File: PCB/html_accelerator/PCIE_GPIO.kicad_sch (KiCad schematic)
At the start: 31 parts, among them U1 MCS9990, U3 CAT24C256YI-GT3, Y1 12MHz

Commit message: placement updates
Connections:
- net at R20.2, U1.29 (EE_SCL): now also U3.5 (SDA); no longer U3.6 (SCL)
- net at R20.2, U1.30 (EE_SDA): now also U3.6 (SCL); no longer U3.5 (SDA)
- net +3V3 renamed 3v3_filt
- net 3v3_filt: no longer R20.1
- new net +3V0: R20.1
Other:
- moved on the sheet: U3
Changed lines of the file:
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@@
     (stroke (width 0) (type default))
   )
+  (wire (pts (xy 41.91 25.4) (xy 40.64 25.4))
+    (stroke (width 0) (type default))
+  )
   (wire (pts (xy 40.64 41.91) (xy 40.64 53.34))
     (stroke (width 0) (type default))
@@
     (stroke (width 0) (type default))
   )
-  (wire (pts (xy 52.07 87.63) (xy 52.07 74.93))
+  (wire (pts (xy 52.07 73.66) (xy 52.07 87.63))
     (stroke (width 0) (type default))
   )
@@
     (stroke (width 0) (type default))
   )
-  (image (at 233.68 127) (scale 0.458951)
+  (image (at 233.68 127) (scale 0.972527)
     (data
       iVBORw0KGgoAAAANSUhEUgAAAt0AAAOOCAIAAABTODlIAAAAA3NCSVQICAjb4U/gAAAACXBIWXMA
-      ABYlAAAWJQFJUiTwAAAgAElEQVR4nOy9d9RlZXn3/7nusvcpz/NMowxtQECKUsSIXV9jNGLBgqiJ
+      ABXgAAAV4AGNVCw4AAAgAElEQVR4nOy9d9RlZXn3/7nusvcpz/NMowxtQECKUsSIXV9jNGLBgqiJ
       WBMTTTQWfDVGowaN4muiBhWx99hQCRYUIqiAKCJNijC0oTjDDNOecsred7neP/Y5zzwzQJK1fmv9
       fvhb57vOmvWcffa+275nX9/9va77ukW1D47sASQjGRREcQkiAJ7KksltAAHJYFiEsitkxy8BDLjU
@@
     )
   )
-  (image (at 238.76 73.66) (scale 0.546766)
+  (image (at 238.76 73.66) (scale 1.03777)
     (data
       iVBORw0KGgoAAAANSUhEUgAAAuwAAAE8CAIAAAAUlHMZAAAAA3NCSVQICAjb4U/gAAAACXBIWXMA
-      ABYlAAAWJQFJUiTwAAAgAElEQVR4nOy9ebwuR1ku+rxvVXV/31p7Z+9MEBISAZmUyxgwSgBFwQBX
+      ABXgAAAV4AGNVCw4AAAgAElEQVR4nOy9ebwuR1ku+rxvVXV/31p7Z+9MEBISAZmUyxgwSgBFwQBX
       HPDAUS8cjwiCGjgc1CCIHhSUweBlSnAERBEZhJigEoTILAQQEwhDIhCGE5LsZI9rfV93V9X7nj+q
       eviGtXeAyPV37ee3f3ut1V1dXVVdw1PP+1YVqUYAUAYABQgAlCAAIIBwuqaAcLoL4kg5LAOkAdB0
@@
     (effects (font (size 1.27 1.27)) (justify left bottom))
   )
-  (symbol (lib_id "power:+3V3") (at 40.64 25.4 0) (unit 1)
-    (in_bom yes) (on_board yes) (dnp no) (fields_autoplaced)
-    (property "Reference" "#PWR03" (at 40.64 29.21 0)
-      (effects (font (size 1.27 1.27)) hide)
-    )
-    (property "Value" "+3V3a_filt" (at 40.64 21.8981 0)
-      (effects (font (size 1.27 1.27)))
-    )
-    (property "Footprint" "" (at 40.64 25.4 0)
-      (effects (font (size 1.27 1.27)) hide)
-    )
-    (property "Datasheet" "" (at 40.64 25.4 0)
-      (effects (font (size 1.27 1.27)) hide)
-    )
-    (pin "1")
-    (instances
-      (project "html_accelerator"
-        (path "/12b3a7c9-141f-40ba-9ebb-094b58bfa6c7/3421334e-11b3-46c8-b0f2-353f0fa6f362"
-          (reference "#PWR03") (unit 1)
-        )
-        (path "/12b3a7c9-141f-40ba-9ebb-094b58bfa6c7/8c9bd1fc-c6d3-45cd-babe-9d9e8ea6549d"
-          (reference "#PWR051") (unit 1)
-        )
-        (path "/12b3a7c9-141f-40ba-9ebb-094b58bfa6c7/e5de870d-07a3-4698-84b8-c201bbab4843"
-          (reference "#PWR058") (unit 1)
-        )
-      )
+  (global_label "3v3_filt" (shape input) (at 41.91 25.4 0) (fields_autoplaced)
+    (effects (font (size 1.27 1.27)) (justify left))
+    (property "Intersheetrefs" "${INTERSHEET_REFS}" (at 51.8914 25.4 0)
+      (effects (font (size 1.27 1.27)) (justify left))
     )
   )
@@
     (pin "77")
     (pin "78")
+    (pin "81")
+    (pin "82")
     (pin "10")
     (pin "13")
@@
     (pin "54")
     (pin "57")
-    (pin "81")
-    (pin "82")
     (pin "100")
     (pin "102")
@@
     )
   )
-  (symbol (lib_name "MCS9990_1") (lib_id "html_accel_Symbols:MCS9990") (at 82.55 105.41 0) (unit 2)
+  (symbol (lib_id "html_accel_Symbols:MCS9990") (at 82.55 105.41 0) (unit 2)
     (in_bom yes) (on_board yes) (dnp no) (fields_autoplaced)
     (property "Reference" "U1" (at 98.425 101.1106 0)
@@
       (effects (font (size 1.27 1.27)) hide)
     )
-    (property "Datasheet" "5% Tolerance" (at 67.31 130.81 0)
+    (property "Datasheet" "~" (at 67.31 130.81 0)
       (effects (font (size 1.27 1.27)) hide)
     )
@@
     )
   )
-  (symbol (lib_id "power:+3V3") (at 100.33 45.72 0) (unit 1)
-    (in_bom yes) (on_board yes) (dnp no)
-    (property "Reference" "#PWR07" (at 100.33 49.53 0)
-      (effects (font (size 1.27 1.27)) hide)
-    )
-    (property "Value" "+3V3_aux" (at 100.33 42.2181 0)
-      (effects (font (size 1.27 1.27)))
-    )
-    (property "Footprint" "" (at 100.33 45.72 0)
-      (effects (font (size 1.27 1.27)) hide)
-    )
-    (property "Datasheet" "" (at 100.33 45.72 0)
-      (effects (font (size 1.27 1.27)) hide)
-    )
-    (pin "1")
-    (instances
-      (project "html_accelerator"
-        (path "/12b3a7c9-141f-40ba-9ebb-094b58bfa6c7/3421334e-11b3-46c8-b0f2-353f0fa6f362"
-          (reference "#PWR07") (unit 1)
-        )
-        (path "/12b3a7c9-141f-40ba-9ebb-094b58bfa6c7/e5de870d-07a3-4698-84b8-c201bbab4843"
-          (reference "#PWR059") (unit 1)
-        )
-      )
-    )
-  )
   (symbol (lib_id "Device:R_US") (at 69.85 49.53 0) (unit 1)
     (in_bom yes) (on_board yes) (dnp no)
@@
       (effects (font (size 1.27 1.27)) hide)
     )
-    (property "Datasheet" "12M20P2/49SMT" (at 59.69 123.19 0)
+    (property "Datasheet" "~" (at 59.69 123.19 0)
       (effects (font (size 1.27 1.27)) hide)
     )
@@
     )
   )
+  (symbol (lib_id "power:+3V0") (at 100.33 45.72 0) (unit 1)
+    (in_bom yes) (on_board yes) (dnp no) (fields_autoplaced)
+    (property "Reference" "#PWR011" (at 100.33 49.53 0)
+      (effects (font (size 1.27 1.27)) hide)
+    )
+    (property "Value" "+3V3_aux" (at 100.33 42.2181 0)
+      (effects (font (size 1.27 1.27)))
+    )
+    (property "Footprint" "" (at 100.33 45.72 0)
+      (effects (font (size 1.27 1.27)) hide)
+    )
+    (property "Datasheet" "" (at 100.33 45.72 0)
+      (effects (font (size 1.27 1.27)) hide)
+    )
+    (pin "1")
+    (instances
+      (project "html_accelerator"
+        (path "/12b3a7c9-141f-40ba-9ebb-094b58bfa6c7/3421334e-11b3-46c8-b0f2-353f0fa6f362"
+          (reference "#PWR011") (unit 1)
+        )
+        (path "/12b3a7c9-141f-40ba-9ebb-094b58bfa6c7/e5de870d-07a3-4698-84b8-c201bbab4843"
+          (reference "#PWR013") (unit 1)
+        )
+      )
+    )
+  )
   (symbol (lib_id "Device:R_US") (at 115.57 86.36 0) (unit 1)
     (in_bom yes) (on_board yes) (dnp no)
@@
       (effects (font (size 1.27 1.27)))
     )
-    (property "Footprint" "Package_SO:TSSOP-8_4.4x3mm_P0.65mm" (at 52.07 55.88 0)
+    (property "Footprint" "Package_SO:TSSOP-8_4.4x3mm_P0.65mm" (at 49.53 50.8 0)
       (effects (font (size 1.27 1.27)) hide)
     )
-    (property "Datasheet" "https://www.onsemi.cn/PowerSolutions/document/CAT24C256-D.PDF" (at 50.8 63.5 0)
+    (property "Datasheet" "https://www.onsemi.cn/PowerSolutions/document/CAT24C256-D.PDF" (at 52.07 50.8 0)
       (effects (font (size 1.27 1.27)) hide)
     )
@@
       (effects (font (size 1.27 1.27)) hide)
     )
-    (property "Datasheet" "5% tolerance" (at 52.07 130.81 0)
+    (property "Datasheet" "~" (at 52.07 130.81 0)
       (effects (font (size 1.27 1.27)) hide)
     )

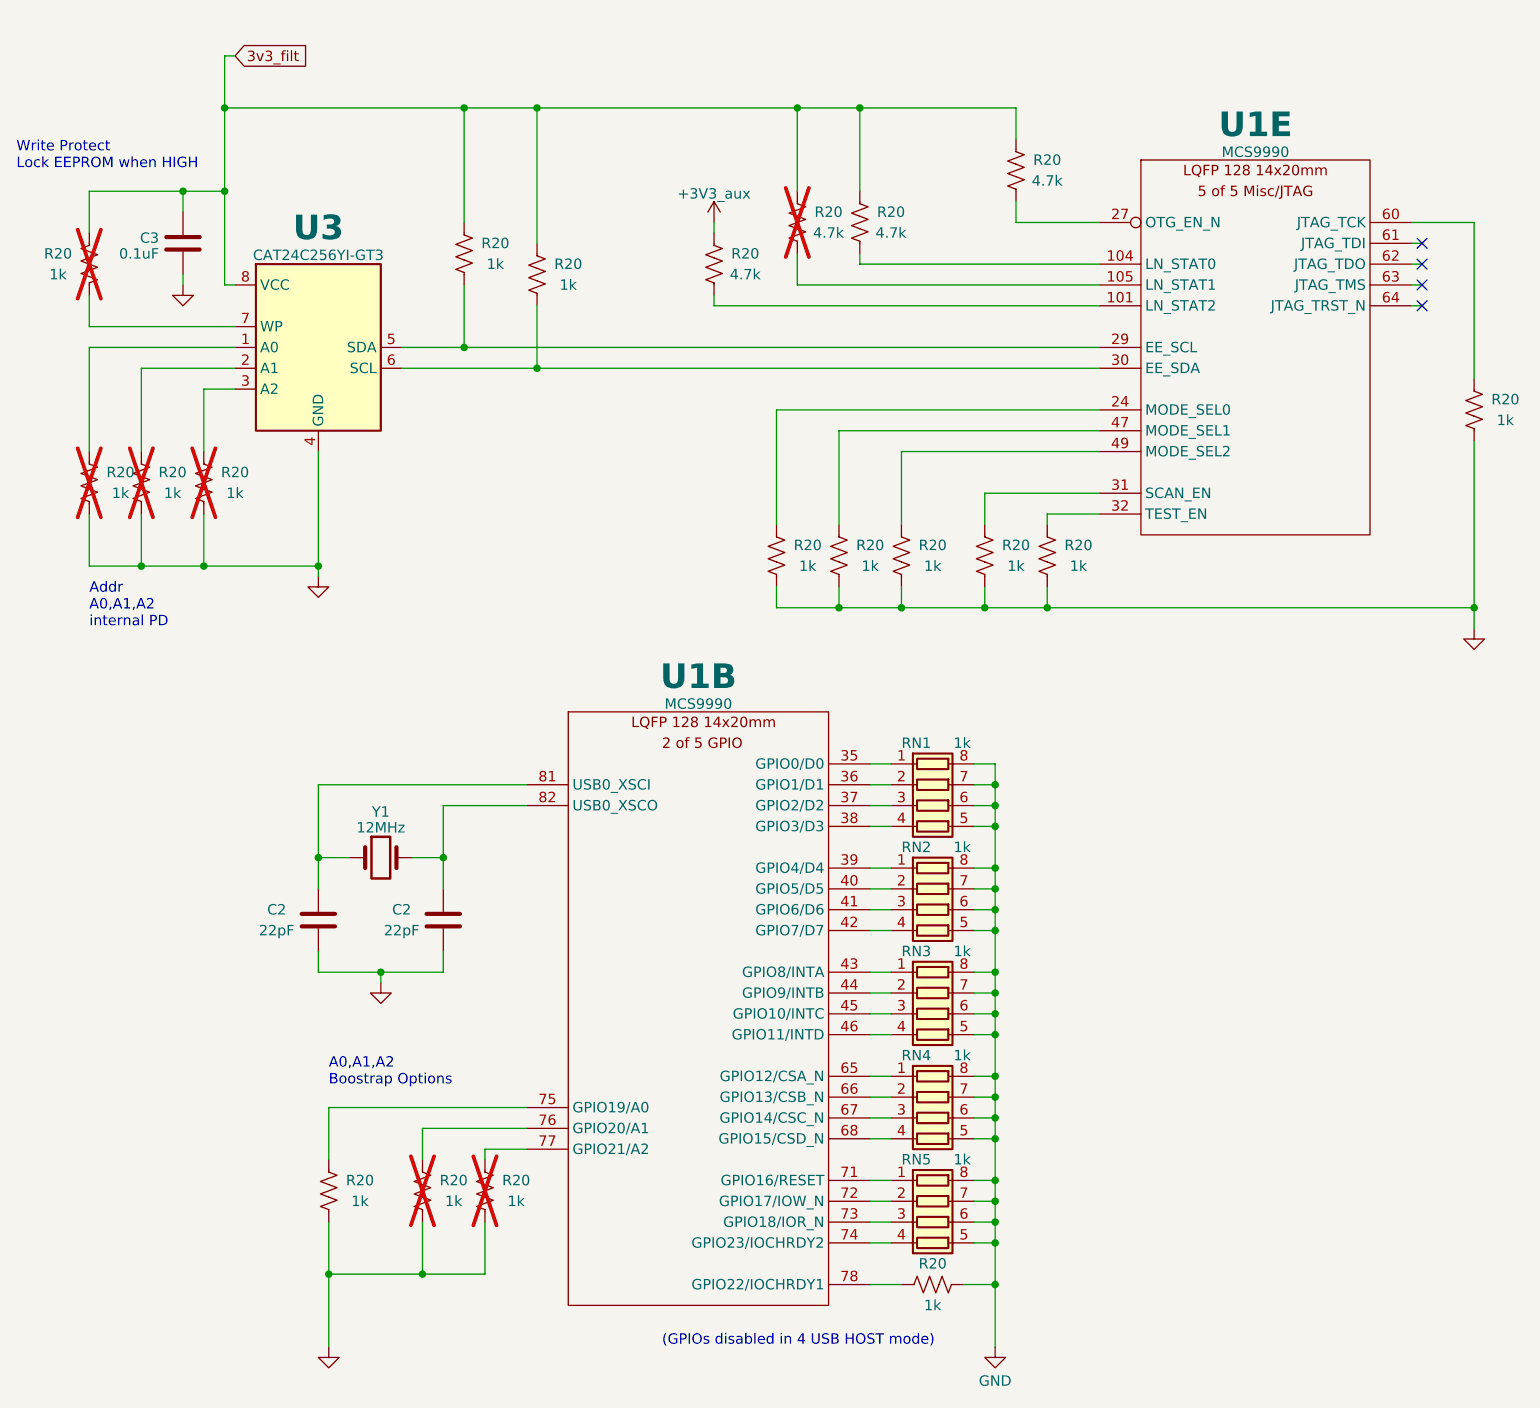
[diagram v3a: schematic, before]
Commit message: constraints for impedance control
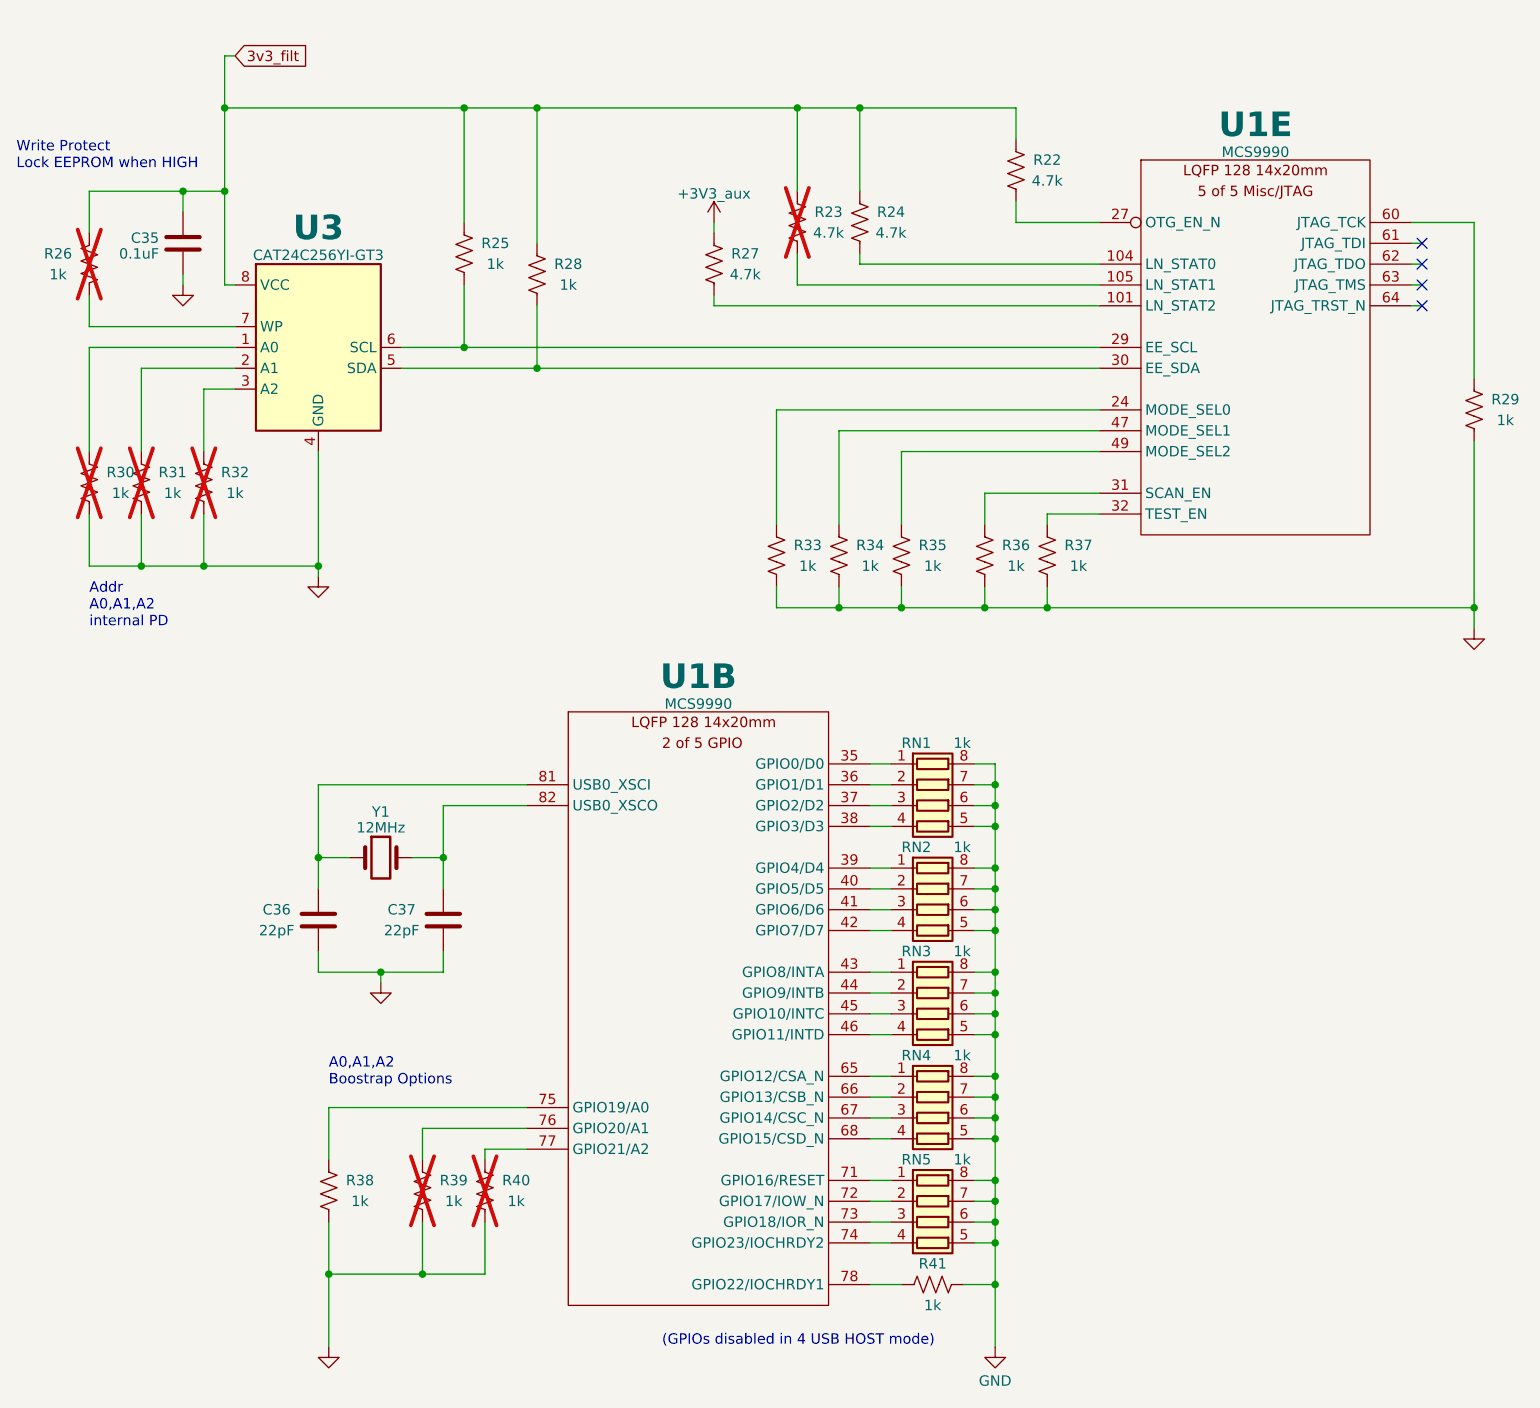
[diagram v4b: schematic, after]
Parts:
- renumbered C3 to C35, C2 to C36, C2 to C37, R20 to R22, R20 to R23, R20 to R24, R20 to R25, R20 to R26, R20 to R27, R20 to R28, R20 to R29, R20 to R30, R20 to R31, R20 to R32, R20 to R33, R20 to R34, R20 to R35, R20 to R36, R20 to R37, R20 to R38, R20 to R39, R20 to R40, R20 to R41
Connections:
- net at R25.2, U1.29 (EE_SCL): now also U3.6 (SCL); no longer U3.5 (SDA)
- net at R28.2, U1.30 (EE_SDA): now also U3.5 (SDA); no longer U3.6 (SCL)
